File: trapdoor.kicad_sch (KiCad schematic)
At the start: 2 parts, among them P9 TRAPDOOR

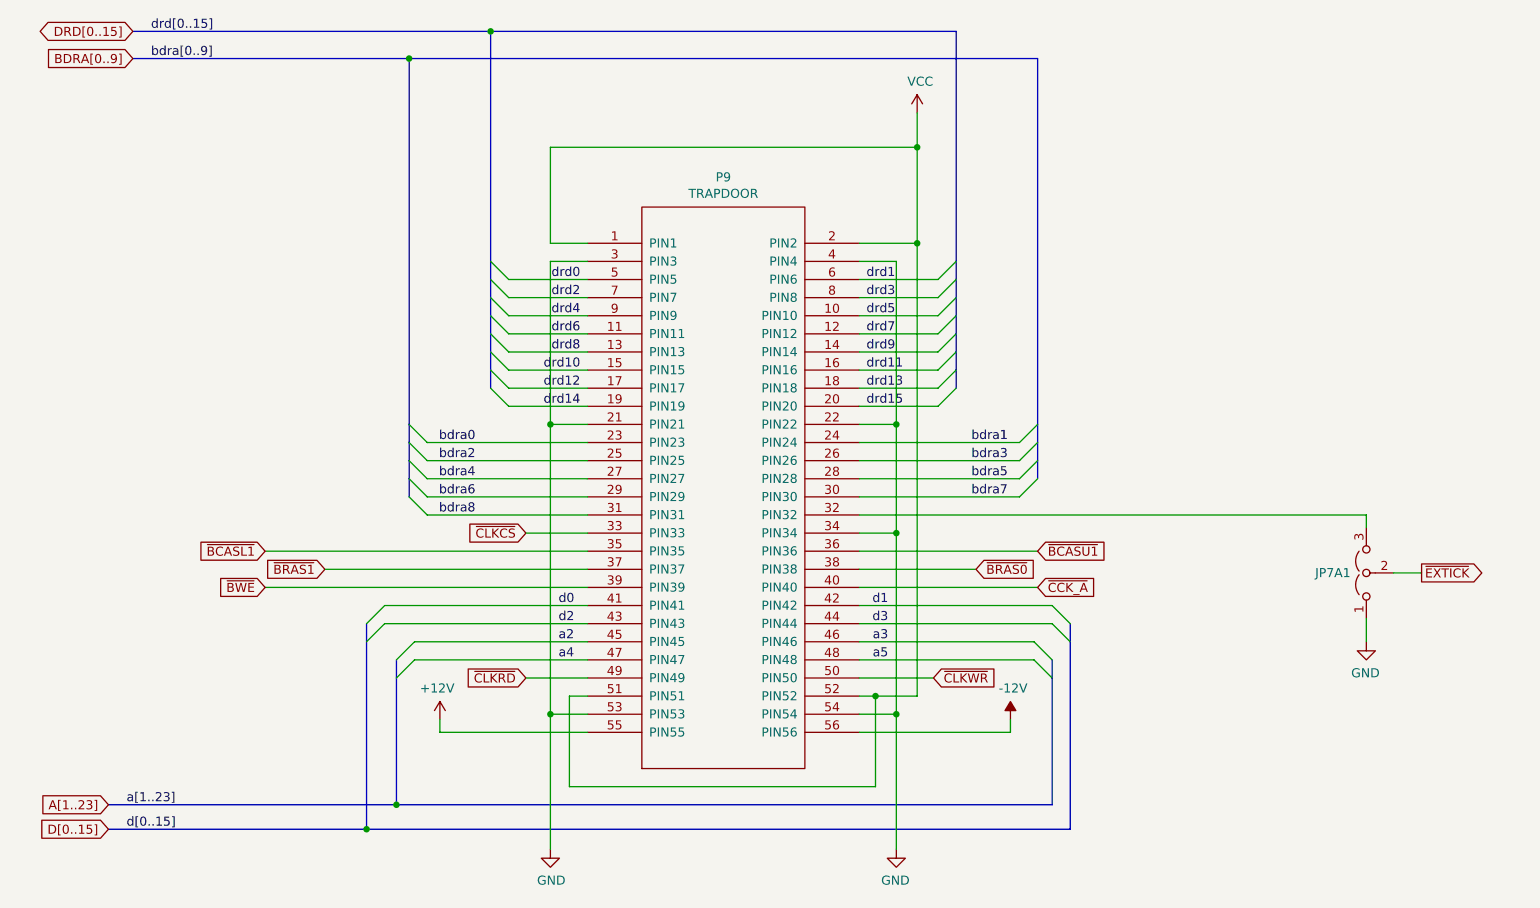
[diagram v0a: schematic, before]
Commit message: DRAM chips replaced with SIMM module
Added logic to decode 2MB chip + 1.5MB slow
Rewired trapdoor slot
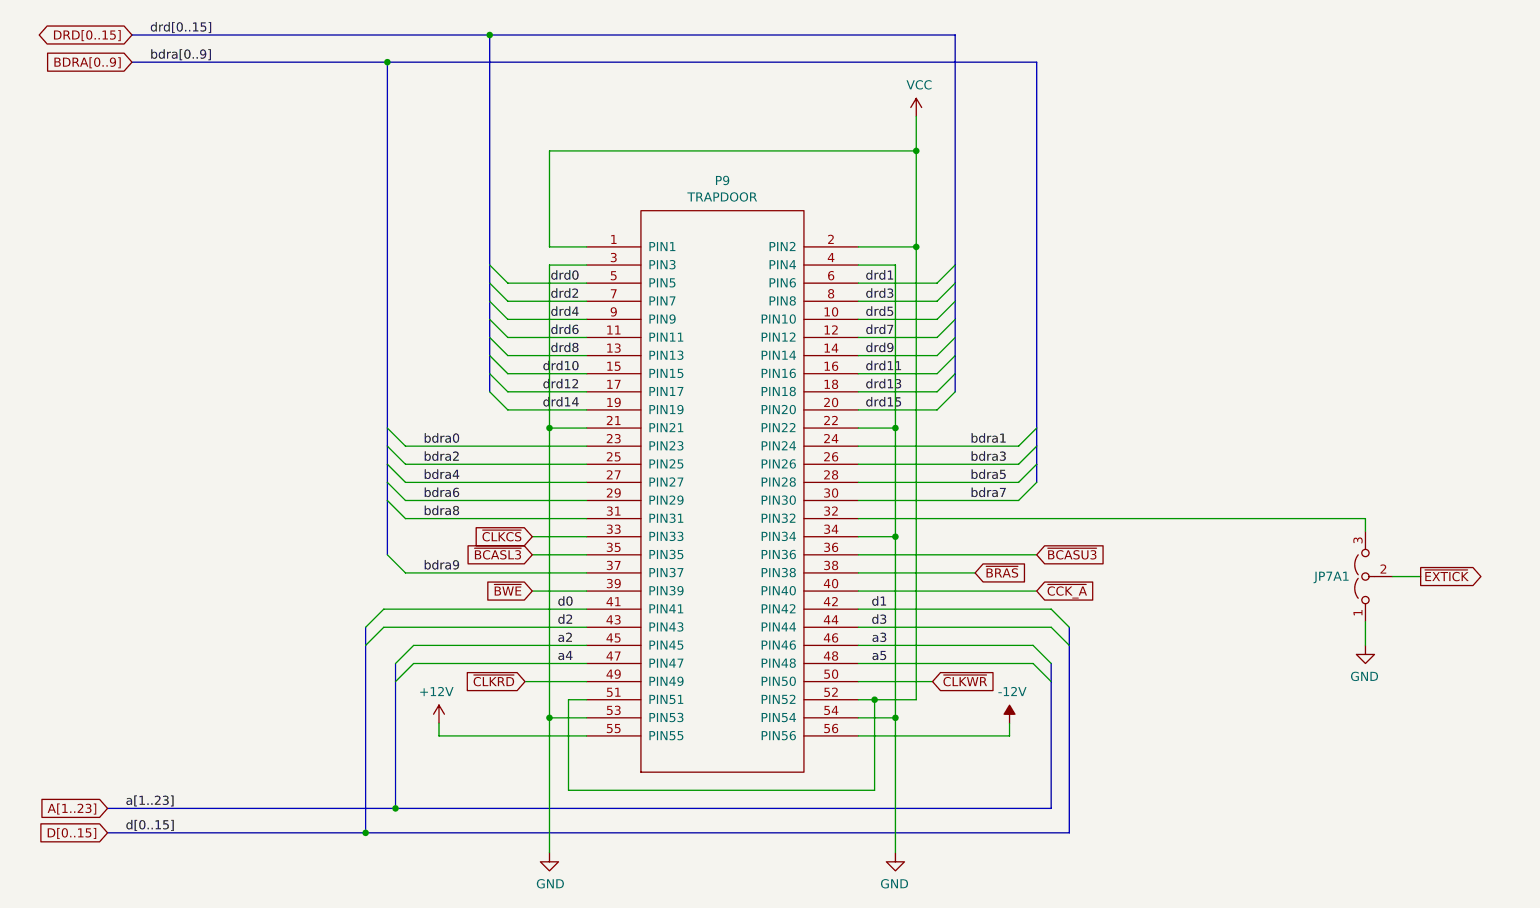
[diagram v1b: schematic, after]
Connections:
- net ~{BCASL1} renamed ~{BCASL3}
- net ~{BCASU1} renamed ~{BCASU3}
- net ~{BRAS0} renamed ~{BRAS}
- net ~{BRAS1} renamed bdra9
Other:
- title: Rämixx500 -> Rämixx500_max
- moved on the sheet: JP7A1, P9

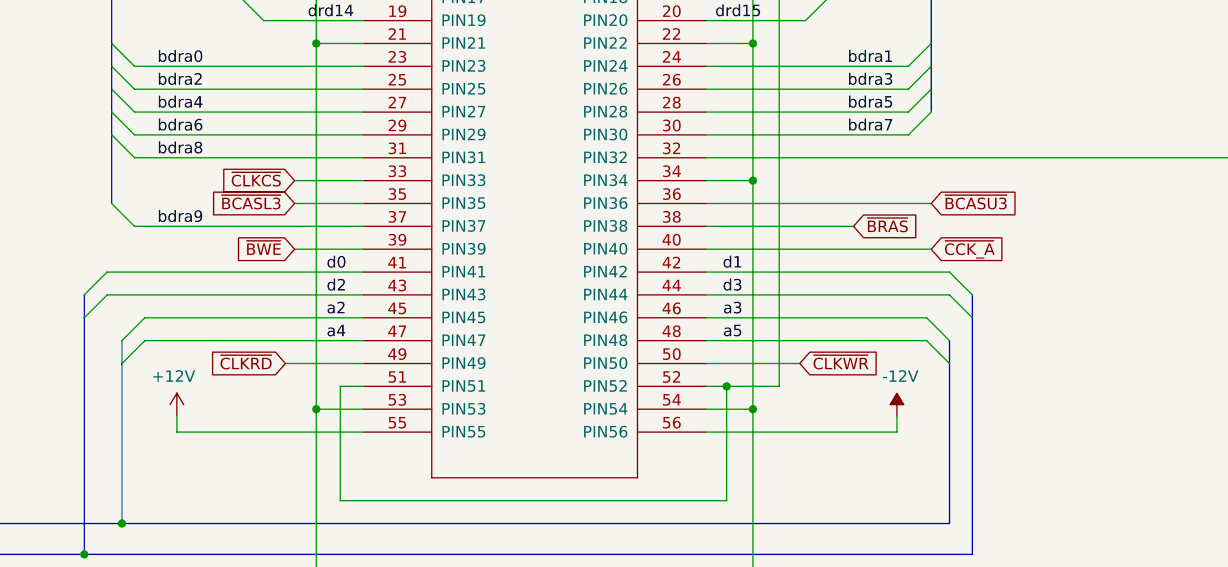
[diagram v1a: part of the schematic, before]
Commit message: optimized timing
removed CCK from RAM buffers to ease routing
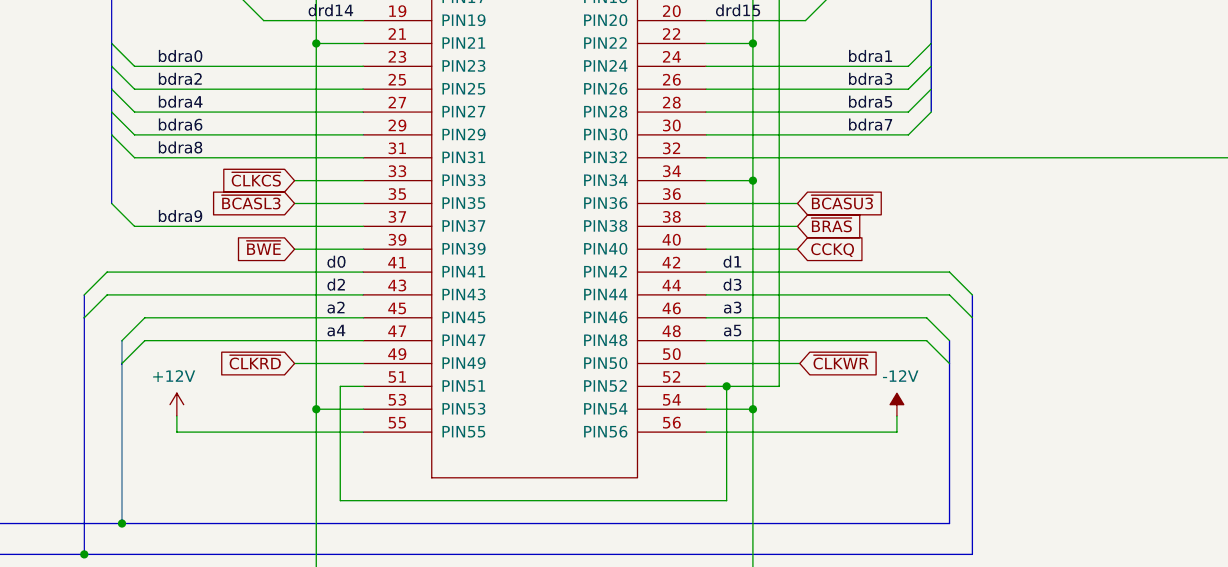
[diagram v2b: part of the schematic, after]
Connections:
- net ~{CCK_A} renamed CCKQ
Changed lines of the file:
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@@
 	(wire
 		(pts
-			(xy 175.26 106.68) (xy 191.643 106.68)
+			(xy 175.26 106.68) (xy 185.42 106.68)
 		)
 		(stroke
@@
 	(wire
 		(pts
-			(xy 175.26 109.22) (xy 200.279 109.22)
+			(xy 175.26 109.22) (xy 185.42 109.22)
 		)
 		(stroke
@@
 	(wire
 		(pts
-			(xy 128.524 121.92) (xy 137.16 121.92)
+			(xy 129.54 121.92) (xy 137.16 121.92)
 		)
 		(stroke
@@
 	(wire
 		(pts
-			(xy 175.26 104.14) (xy 200.279 104.14)
+			(xy 175.26 104.14) (xy 185.42 104.14)
 		)
 		(stroke
@@
 		)
 	)
-	(global_label "~{CCK_A}"
+	(global_label "CCKQ"
 		(shape input)
-		(at 200.279 109.22 0)
+		(at 185.42 109.22 0)
 		(effects
 			(font
@@
 		)
 		(property "Intersheetrefs" "${INTERSHEET_REFS}"
-			(at 200.279 109.22 0)
+			(at 185.42 109.22 0)
 			(effects
 				(font
@@
 	(global_label "~{CLKRD}"
 		(shape input)
-		(at 128.524 121.92 180)
+		(at 129.54 121.92 180)
 		(effects
 			(font
@@
 		)
 		(property "Intersheetrefs" "${INTERSHEET_REFS}"
-			(at 128.524 121.92 0)
+			(at 129.54 121.92 0)
 			(effects
 				(font
@@
 	(global_label "~{BCASU3}"
 		(shape input)
-		(at 200.279 104.14 0)
+		(at 185.42 104.14 0)
 		(effects
 			(font
@@
 		)
 		(property "Intersheetrefs" "${INTERSHEET_REFS}"
-			(at 200.279 104.14 0)
+			(at 185.42 104.14 0)
 			(effects
 				(font
@@
 	(global_label "~{BRAS}"
 		(shape input)
-		(at 191.643 106.68 0)
+		(at 185.42 106.68 0)
 		(effects
 			(font
@@
 		)
 		(property "Intersheetrefs" "${INTERSHEET_REFS}"
-			(at 191.643 106.68 0)
-			(effects
-				(font
+			(at 185.42 106.68 0)
+			(effects
+				(font

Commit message: removed JP2
some more small fixes
schematic is now more or less done I think
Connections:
- net CCKQ renamed ~{CCK_A}
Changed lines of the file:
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@@
 		)
 	)
-	(global_label "CCKQ"
+	(global_label "~{CCK_A}"
 		(shape input)
 		(at 185.42 109.22 0)

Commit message: Started cleaning up BOM
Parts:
- JP7A1: now left out of the parts list
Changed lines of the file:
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@@
 		(unit 1)
 		(exclude_from_sim no)
-		(in_bom yes)
+		(in_bom no)
 		(on_board yes)
 		(dnp no)
